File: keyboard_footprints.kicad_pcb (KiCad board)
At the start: 2 copper layers, 74.5 x 38 mm, 7 parts

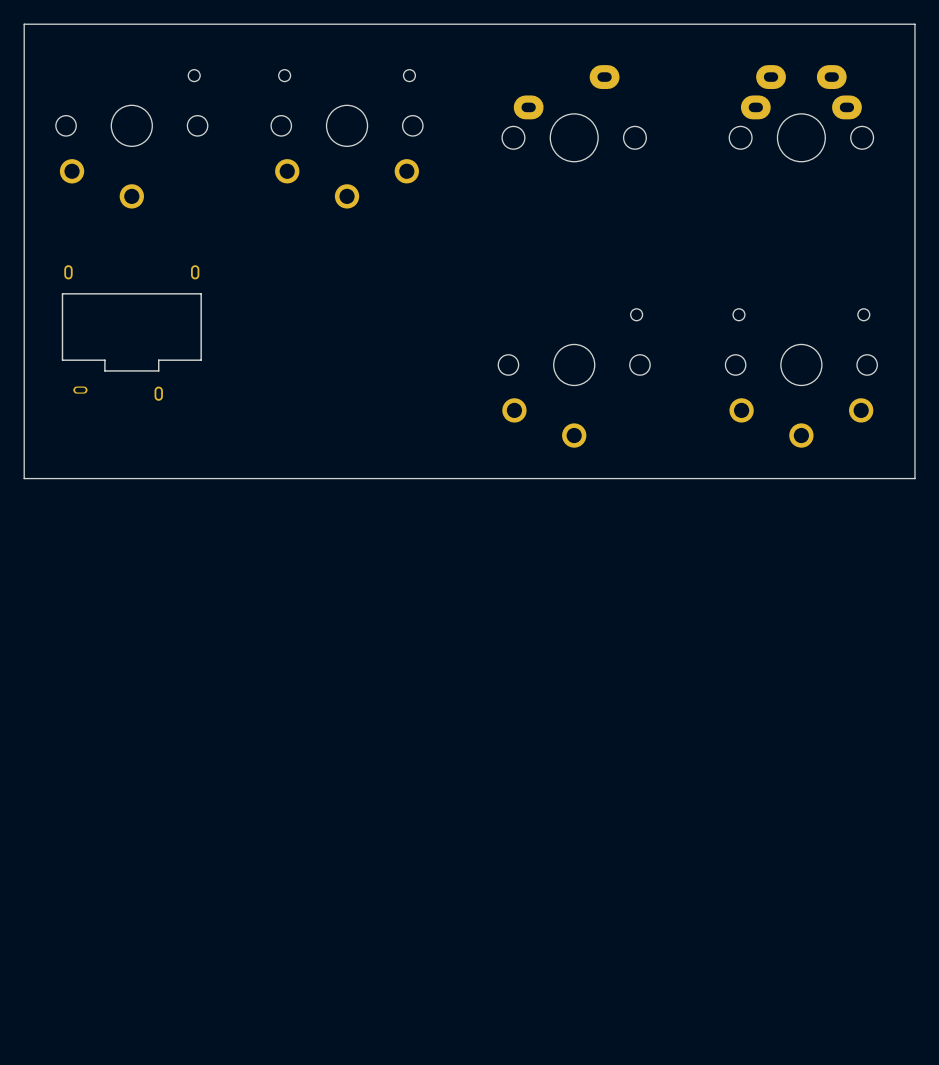
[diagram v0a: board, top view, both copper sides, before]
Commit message: Add other miscellaneous footprints I use
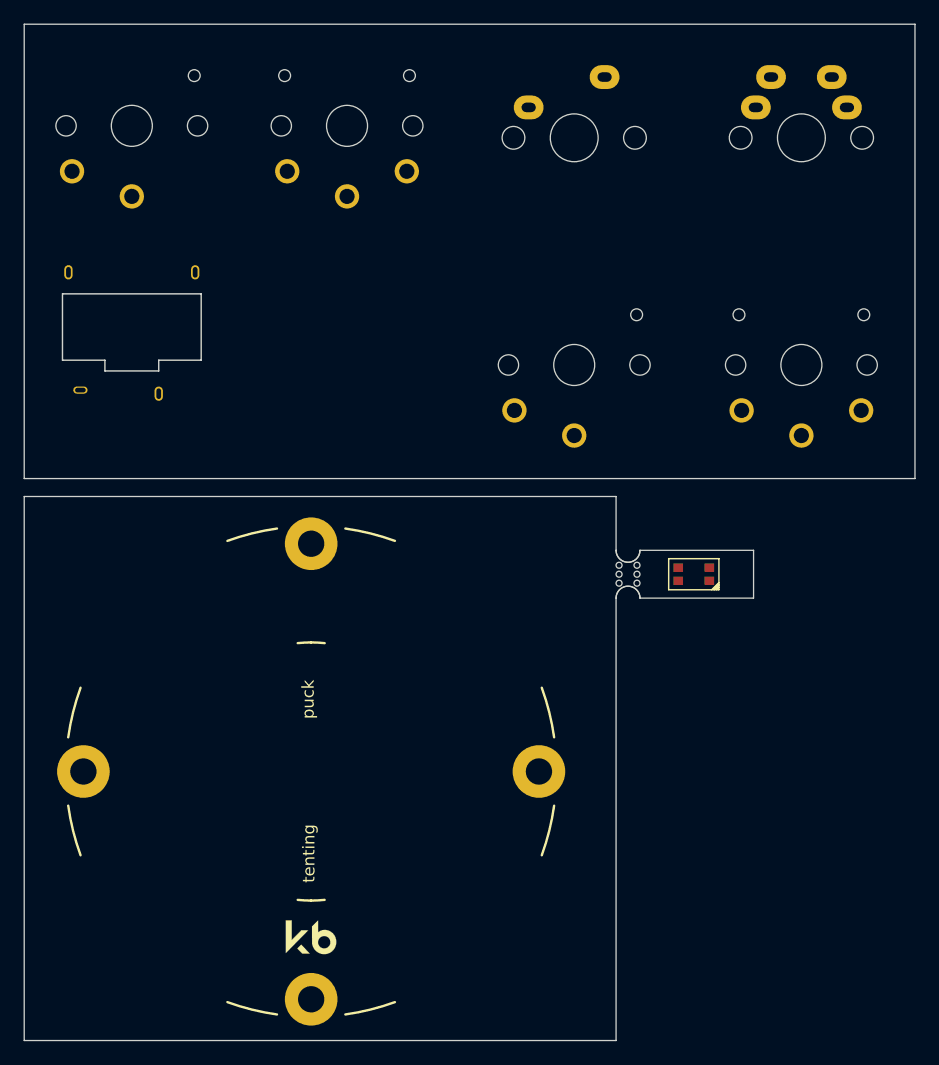
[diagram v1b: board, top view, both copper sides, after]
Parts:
- added REF**: FM-B2020RGBA-HG, rgb:LED_RGB_FM-B2020RGBA-HG, F.Cu at (68.0, 58.5)
- added REF**: Tenting Puck, puck:Tenting_Puck, F.Cu at (36.0, 75.0)
- added mouse-bite-2mm-slot: VAL**, panelization:mouse-bite-2mm-slot, F.Cu at (62.5, 58.5)
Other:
- board size 74.5 x 38 mm -> 74.5 x 85 mm

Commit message: Add 2mm mouse bite with space for a track
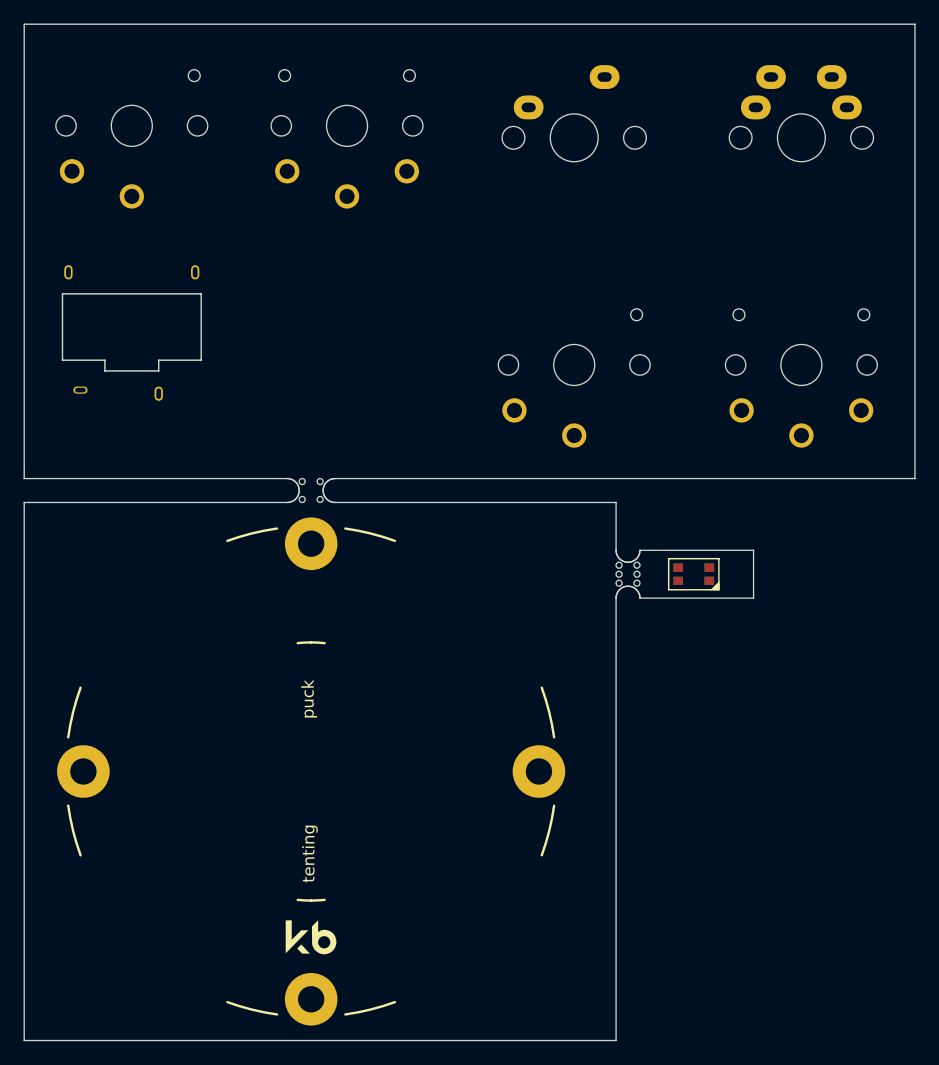
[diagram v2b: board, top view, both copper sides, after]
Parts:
- added REF**: mouse-bite-2mm-slot-with-space-for-track, panelization:mouse-bite-2mm-slot-with-space-for-track, F.Cu at (36.0, 51.5)
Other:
- outline, holes or cut-outs redrawn
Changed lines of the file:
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@@
   (general
     (thickness 1.6)
-    (drawings 14)
+    (drawings 18)
     (tracks 0)
     (zones 0)
-    (modules 10)
+    (modules 11)
     (nets 1)
   )
@@
     (uvia_dia 0.3)
     (uvia_drill 0.1)
+  )
+  (module panelization:mouse-bite-2mm-slot-with-space-for-track (layer F.Cu)
+    (at 36 51.5)
+    (fp_text reference REF** (at 0 0.5) (layer F.SilkS) hide
+      (effects (font (size 1 1) (thickness 0.15)))
+    )
+    (fp_text value mouse-bite-2mm-slot-with-space-for-track (at 0 -0.5) (layer F.Fab) hide
+      (effects (font (size 1 1) (thickness 0.15)))
+    )
+    (fp_arc (start 2 0) (end 2 1) (angle 180) (layer F.SilkS) (width 0.1))
+    (fp_arc (start -2 0) (end -2 -1) (angle 180) (layer F.SilkS) (width 0.1))
+    (fp_line (start -2 0) (end -2 0) (layer Eco1.User) (width 2))
+    (fp_line (start 2 0) (end 2 0) (layer Eco1.User) (width 2))
+    (fp_circle (center -2 0) (end -2 -0.06) (layer Dwgs.User) (width 0.05))
+    (fp_circle (center 2 0) (end 2.06 0) (layer Dwgs.User) (width 0.05))
+    (pad "" np_thru_hole circle (at 0.75 -0.75) (size 0.5 0.5) (drill 0.5) (layers *.Cu *.Mask))
+    (pad "" np_thru_hole circle (at 0.75 0.75) (size 0.5 0.5) (drill 0.5) (layers *.Cu *.Mask))
+    (pad "" np_thru_hole circle (at -0.75 0.75) (size 0.5 0.5) (drill 0.5) (layers *.Cu *.Mask))
+    (pad "" np_thru_hole circle (at -0.75 -0.75) (size 0.5 0.5) (drill 0.5) (layers *.Cu *.Mask))
   )
   (module panelization:mouse-bite-2mm-slot (layer F.Cu)
@@
       (clearance 0.2))
   )
+  (gr_arc (start 38 51.5) (end 38 50.5) (angle -180) (layer Edge.Cuts) (width 0.05))
+  (gr_arc (start 34 51.5) (end 34 52.5) (angle -180) (layer Edge.Cuts) (width 0.05))
+  (gr_line (start 34 52.5) (end 12 52.5) (layer Edge.Cuts) (width 0.05))
+  (gr_line (start 61.5 52.5) (end 38 52.5) (layer Edge.Cuts) (width 0.05))
+  (gr_line (start 38 50.5) (end 86.5 50.5) (layer Edge.Cuts) (width 0.05))
   (gr_arc (start 62.5 56.5) (end 61.5 56.5) (angle -180) (layer Edge.Cuts) (width 0.05))
   (gr_arc (start 62.5 60.5) (end 63.5 60.5) (angle -180) (layer Edge.Cuts) (width 0.05))
   (gr_line (start 61.5 97.5) (end 61.5 60.5) (layer Edge.Cuts) (width 0.05))
   (gr_line (start 12 97.5) (end 61.5 97.5) (layer Edge.Cuts) (width 0.05))
-  (gr_line (start 12 52) (end 12 97.5) (layer Edge.Cuts) (width 0.05))
-  (gr_line (start 61.5 52) (end 12 52) (layer Edge.Cuts) (width 0.05))
-  (gr_line (start 61.5 56.5) (end 61.5 52) (layer Edge.Cuts) (width 0.05))
+  (gr_line (start 12 52.5) (end 12 97.5) (layer Edge.Cuts) (width 0.05))
+  (gr_line (start 61.5 56.5) (end 61.5 52.5) (layer Edge.Cuts) (width 0.05))
   (gr_line (start 73 60.5) (end 73 56.5) (layer Edge.Cuts) (width 0.05))
   (gr_line (start 63.5 60.5) (end 73 60.5) (layer Edge.Cuts) (width 0.05))
   (gr_line (start 63.5 56.5) (end 73 56.5) (layer Edge.Cuts) (width 0.05))
   (gr_line (start 12 50.5) (end 12 12.5) (layer Edge.Cuts) (width 0.05))
-  (gr_line (start 86.5 50.5) (end 12 50.5) (layer Edge.Cuts) (width 0.05))
+  (gr_line (start 34 50.5) (end 12 50.5) (layer Edge.Cuts) (width 0.05))
   (gr_line (start 86.5 12.5) (end 86.5 50.5) (layer Edge.Cuts) (width 0.05))
   (gr_line (start 12 12.5) (end 86.5 12.5) (layer Edge.Cuts) (width 0.05))
